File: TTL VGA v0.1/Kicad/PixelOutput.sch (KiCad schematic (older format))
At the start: 0 parts

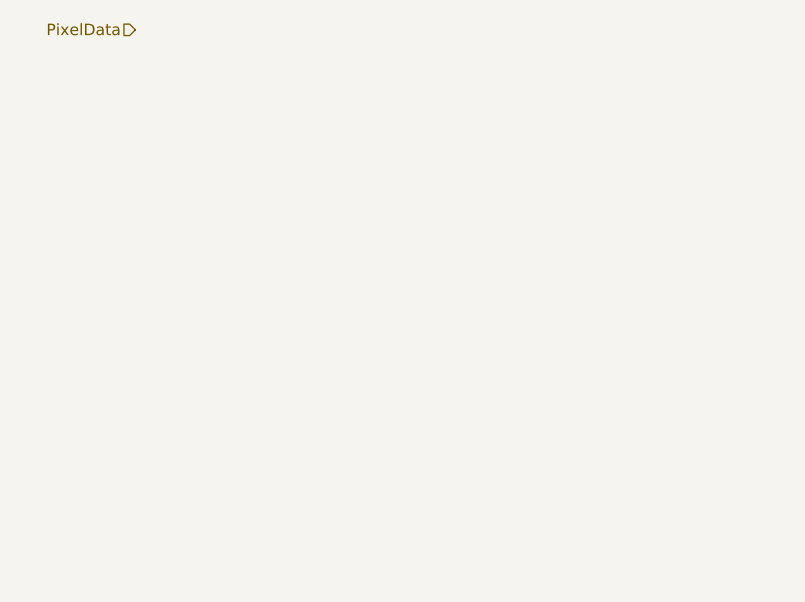
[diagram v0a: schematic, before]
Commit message: vga memory interface
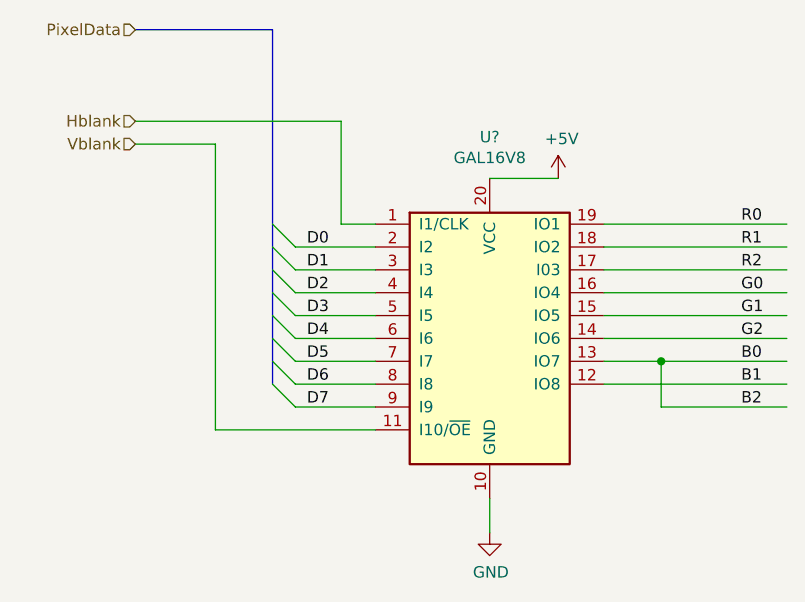
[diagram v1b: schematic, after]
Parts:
- added U?: GAL16V8, symbol Logic_Programmable:GAL16V8
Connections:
- net labels added: +5V, B0, B1, B2, D0, D1, D2, D3, D4, D5, D6, D7, G0, G1, G2, GND, Hblank, R0, R1, R2, Vblank
- wire segments 0 -> 27
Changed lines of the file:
@@
 Text HLabel 1900 1900 0    50   Input ~ 0
 PixelData
+Text HLabel 1900 2300 0    50   Input ~ 0
+Hblank
+Text HLabel 1900 2400 0    50   Input ~ 0
+Vblank
+$Comp
+L Logic_Programmable:GAL16V8 U?
+U 1 1 5E5571A5
+P 3450 3250
+F 0 "U?" H 3450 4131 50  0000 C CNN
+F 1 "GAL16V8" H 3450 4040 50  0000 C CNN
+F 2 "" H 3450 3250 50  0001 C CNN
+F 3 "" H 3450 3250 50  0001 C CNN
+	1    3450 3250
+	1    0    0    -1
+$EndComp
+Wire Wire Line
+	2950 2850 2600 2850
+Wire Wire Line
+	2950 2950 2600 2950
+Wire Wire Line
+	2950 3050 2600 3050
+Wire Wire Line
+	2950 3150 2600 3150
+Wire Wire Line
+	2950 3250 2600 3250
+Wire Wire Line
+	2950 3350 2600 3350
+Wire Wire Line
+	2950 3450 2600 3450
+Wire Wire Line
+	2950 3550 2600 3550
+Text Label 2650 2850 0    50   ~ 0
+D0
+Text Label 2650 2950 0    50   ~ 0
+D1
+Text Label 2650 3050 0    50   ~ 0
+D2
+Text Label 2650 3150 0    50   ~ 0
+D3
+Text Label 2650 3250 0    50   ~ 0
+D4
+Text Label 2650 3350 0    50   ~ 0
+D5
+Text Label 2650 3450 0    50   ~ 0
+D6
+Text Label 2650 3550 0    50   ~ 0
+D7
+Entry Wire Line
+	2500 2750 2600 2850
+Entry Wire Line
+	2500 2850 2600 2950
+Entry Wire Line
+	2500 2950 2600 3050
+Entry Wire Line
+	2500 3050 2600 3150
+Entry Wire Line
+	2500 3150 2600 3250
+Entry Wire Line
+	2500 3250 2600 3350
+Entry Wire Line
+	2500 3350 2600 3450
+Entry Wire Line
+	2500 3450 2600 3550
+Wire Bus Line
+	1900 1900 2500 1900
+Wire Wire Line
+	1900 2300 2800 2300
+Wire Wire Line
+	2800 2300 2800 2750
+Wire Wire Line
+	2800 2750 2950 2750
+Wire Wire Line
+	1900 2400 2250 2400
+Wire Wire Line
+	2250 2400 2250 3650
+Wire Wire Line
+	2250 3650 2950 3650
+$Comp
+L power:GND #PWR?
+U 1 1 5E55AA51
+P 3450 4100
+F 0 "#PWR?" H 3450 3850 50  0001 C CNN
+F 1 "GND" H 3455 3927 50  0000 C CNN
+F 2 "" H 3450 4100 50  0001 C CNN
+F 3 "" H 3450 4100 50  0001 C CNN
+	1    3450 4100
+	1    0    0    -1
+$EndComp
+Wire Wire Line
+	3450 4100 3450 3950
+$Comp
+L power:+5V #PWR?
+U 1 1 5E55AF97
+P 3750 2550
+F 0 "#PWR?" H 3750 2400 50  0001 C CNN
+F 1 "+5V" H 3765 2723 50  0000 C CNN
+F 2 "" H 3750 2550 50  0001 C CNN
+F 3 "" H 3750 2550 50  0001 C CNN
+	1    3750 2550
+	1    0    0    -1
+$EndComp
+Wire Wire Line
+	3750 2550 3450 2550
+Wire Wire Line
+	3950 2750 4750 2750
+Wire Wire Line
+	3950 2850 4750 2850
+Wire Wire Line
+	3950 2950 4750 2950
+Wire Wire Line
+	3950 3050 4750 3050
+Wire Wire Line
+	3950 3150 4750 3150
+Wire Wire Line
+	3950 3250 4750 3250
+Wire Wire Line
+	3950 3350 4200 3350
+Wire Wire Line
+	3950 3450 4750 3450
+Text Label 4550 2750 0    50   ~ 0
+R0
+Text Label 4550 2850 0    50   ~ 0
+R1
+Text Label 4550 2950 0    50   ~ 0
+R2
+Text Label 4550 3050 0    50   ~ 0
+G0
+Text Label 4550 3150 0    50   ~ 0
+G1
+Text Label 4550 3250 0    50   ~ 0
+G2
+Text Label 4550 3350 0    50   ~ 0
+B0
+Text Label 4550 3450 0    50   ~ 0
+B1
+Text Label 4550 3550 0    50   ~ 0
+B2
+Wire Wire Line
+	4200 3350 4200 3550
+Connection ~ 4200 3350
+Wire Wire Line
+	4200 3350 4750 3350
+Wire Wire Line
+	4200 3550 4750 3550
+Wire Bus Line
+	2500 1900 2500 3450
 $EndSCHEMATC
